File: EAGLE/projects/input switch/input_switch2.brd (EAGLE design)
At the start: 50 x 100 mm, 53 parts, among them U1 NE5532AD8G, U2 NE5532AD8G

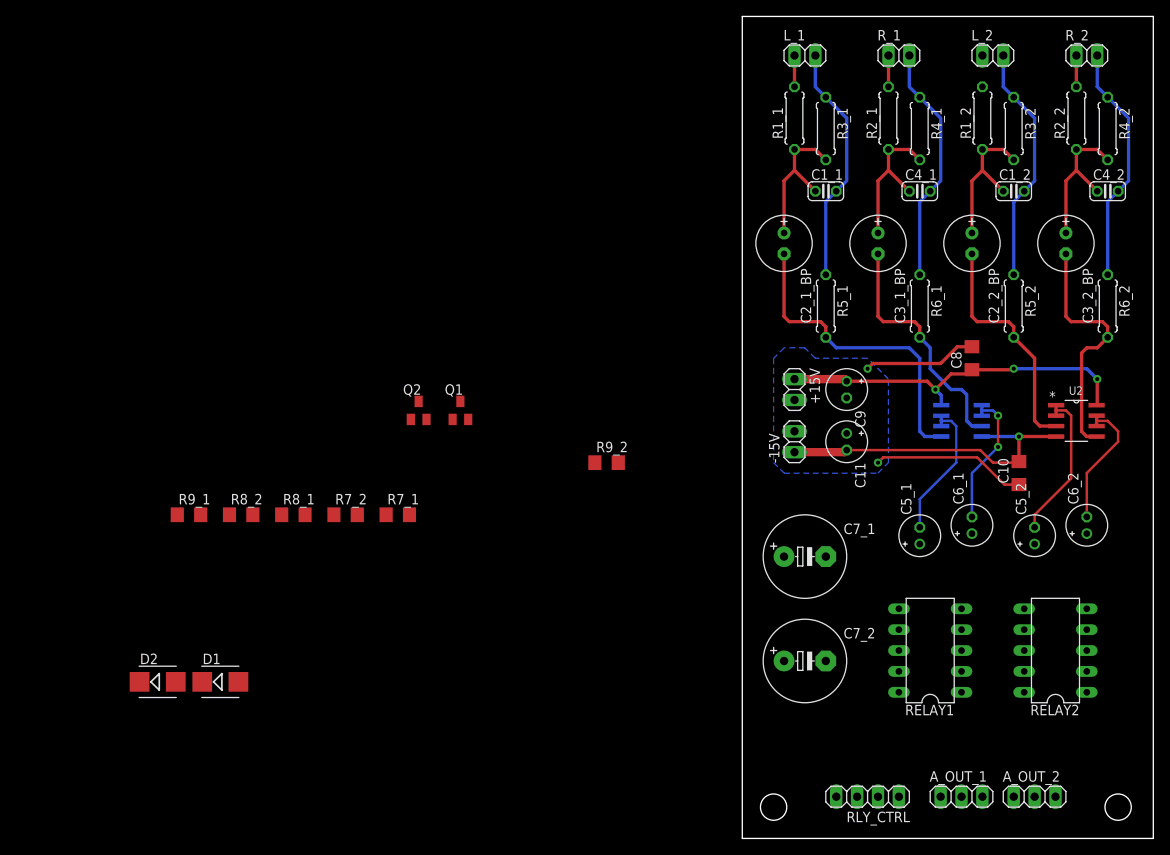
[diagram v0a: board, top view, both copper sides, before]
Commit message: DIP NE5532
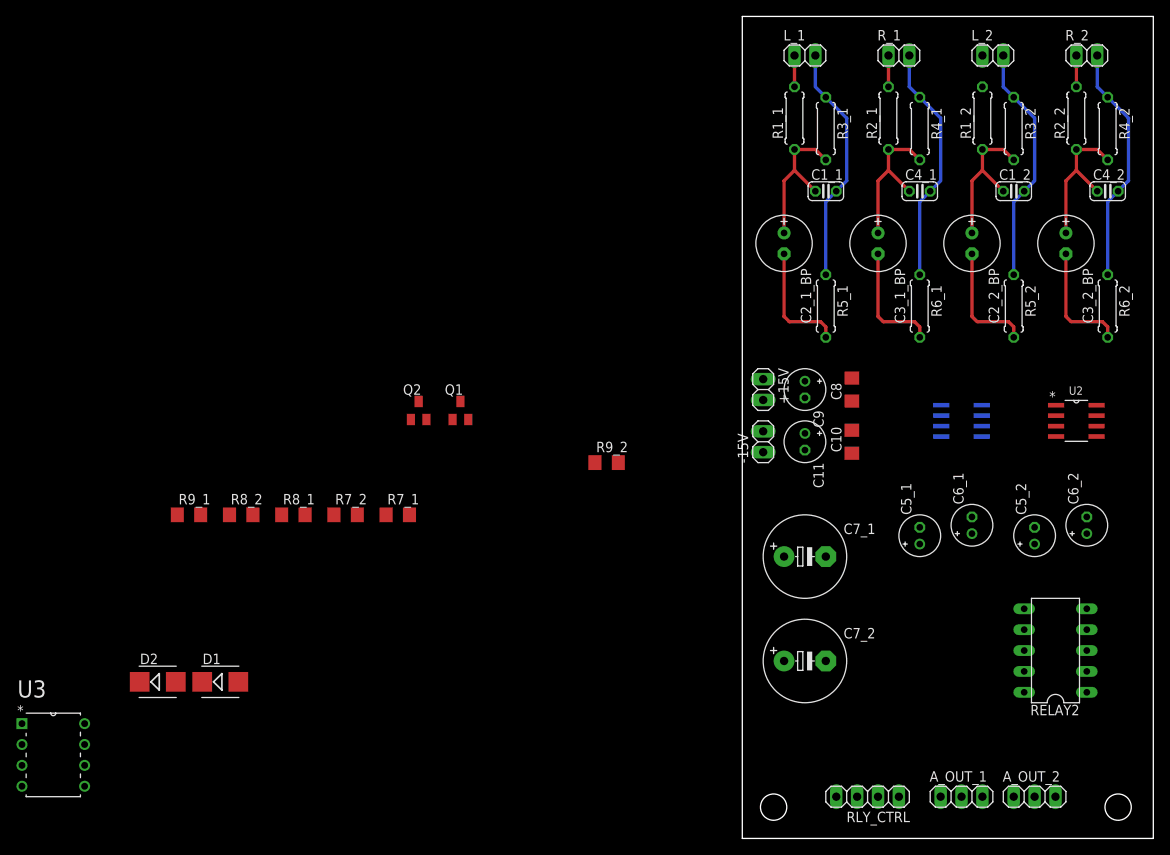
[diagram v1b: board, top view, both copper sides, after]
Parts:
- removed RELAY1: (no value), ic-package:DIL10
- added U3: NE5532P, ne5532:DIP254P762X508-8
- moved C10 20.7 mm to (13.3, 48.3)
- moved C8 15.1 mm to (13.3, 54.6)
- moved C11 5.08 mm to (7.62, 48.3)
- moved C9 5.08 mm to (7.62, 54.6)
- moved +15V 3.81 mm to (2.54, 54.6)
- moved -15V 3.81 mm to (2.54, 48.3)
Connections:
- removed net N$25: A_OUT_1.1, RELAY1.7
- removed net N$8: C6_1.+, RELAY1.3
- new net VCC+: U3.8
- new net VCC-: U3.4
- net N$11: no longer RELAY1.2
- net N$12: no longer RELAY1.9
- net N$18: no longer RELAY1.10
- net N$31: no longer RELAY1.8
- net N$37: no longer RELAY1.1
- net N$9: no longer RELAY1.4
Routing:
- net +15V: track 44.3 -> 0.00 mm, vias 3 -> 0
- net -15V: track 40.2 -> 0.00 mm, vias 1 -> 0
- net GND: track 149.8 -> 117.2 mm, vias 2 -> 0
- net N$4: track 38.7 -> 14.5 mm
- net N$13: track 18.8 -> 0.00 mm
- net N$5: track 17.5 -> 0.00 mm
- net N$7: track 17.1 -> 0.00 mm, vias 2 -> 0
- net N$10: track 16.4 -> 0.00 mm
- net N$26: track 30.1 -> 14.5 mm
- net N$20: track 29.9 -> 14.5 mm
- net N$27: track 28.6 -> 14.5 mm
- removed copper zone on layer 16, net GND

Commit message: input
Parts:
- removed C7_1, C7_2: 220u, rcl:E5-10,5
- removed U3: NE5532P, ne5532:DIP254P762X508-8
- added RELAY1: (no value), ic-package:DIL10
- added RGND1, RGND2, RGND3, RGND4: 10, rcl:R1206
- added R_PS1, R_PS2: 100, rcl:0207/7
- U1, U2: value NE5532AD8G -> NE5532P; device ne5532:SOIC127P600X175-8N -> ne5532:DIP254P762X508-8
- moved R8_2 112.9 mm to (47.0, 6.35), turned to 90 degrees
- moved D2 109.5 mm to (38.1, 26.7)
- moved R9_1 101.2 mm to (27.9, 5.08), turned to 90 degrees
- moved R8_1 90.1 mm to (29.2, 6.35), turned to 90 degrees
- moved R7_2 86.8 mm to (38.1, 30.5)
- moved D1 81.6 mm to (17.8, 26.7)
- moved R9_2 74.3 mm to (45.7, 5.08), turned to 90 degrees
- moved Q2 70.3 mm to (27.9, 31.8)
- moved Q1 67.7 mm to (27.9, 25.4)
- moved R7_1 60.3 mm to (17.8, 30.5)
- moved C5_1 22.2 mm to (43.2, 41.9)
- moved -15V 19.1 mm to (3.81, 29.2)
- moved C9 18.2 mm to (3.81, 36.8), turned to 0 degrees
- moved C6_2 18.2 mm to (24.1, 41.9)
- moved C10 12.3 mm to (8.89, 36.8), turned to 270 degrees
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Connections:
- removed net VCC+: U3.8
- removed net VCC-: U3.4
- new net AGND: A_OUT_1.2, A_OUT_2.2, C1_2.2, C4_1.2, C4_2.2, R3_2.1, R4_1.1, R4_2.1, R5_1.1, R5_2.1, R6_1.1, R6_2.1, RGND1.1, RGND2.1, RGND3.1, RGND4.1
- new net N$14: A_OUT_1.1, RELAY1.7
- new net N$17: -15V.1, R_PS2.2
- new net N$25: +15V.1, R_PS1.2
- new net N$33: L_1.2, RGND2.2
- new net N$36: RGND1.2, R_1.2
- new net N$41: C1_1.2, R3_1.1
- new net N$42: RGND3.2, R_2.2
- new net N$43: L_2.2, RGND4.2
- new net N$8: C6_1.+, RELAY1.3
- net +15V: now also R_PS1.1; no longer +15V.1
- net -15V: now also R_PS2.1; no longer -15V.1
- net GND: no longer A_OUT_1.2, A_OUT_2.2, C1_1.2, C1_2.2, C4_1.2, C4_2.2, L_1.2, L_2.2, R3_1.1, R3_2.1, R4_1.1, R4_2.1, R5_1.1, R5_2.1, R6_1.1, R6_2.1, R_1.2, R_2.2
- net N$11: now also RELAY1.2
- net N$12: now also RELAY1.9
- net N$18: now also RELAY1.10; no longer C7_1.-
- net N$31: now also RELAY1.8
- net N$37: now also RELAY1.1; no longer C7_1.+, C7_2.+
- net N$38: no longer C7_2.-
- net N$9: now also RELAY1.4
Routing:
- net GND: track 117.2 -> 0.00 mm
- net N$3: track 18.6 -> 0.00 mm
- net N$24: track 18.6 -> 0.00 mm
- net N$23: track 18.6 -> 0.00 mm
- net N$6: track 18.6 -> 0.00 mm
- net N$27: track 14.5 -> 0.00 mm
- net N$26: track 14.5 -> 0.00 mm
- net N$4: track 14.5 -> 0.00 mm
- net N$20: track 14.5 -> 0.00 mm
- net N$21: track 3.81 -> 0.00 mm
- net N$2: track 3.81 -> 0.00 mm
- net N$1: track 3.81 -> 0.00 mm
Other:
- board size 50 x 100 mm -> 49.5 x 99.7 mm

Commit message: Input Board done
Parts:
- added C1, C2: (no value), rcl:C1206
- added J1: J12MM, jumper:12
- added J2: J25MM, jumper:25
- added SJ1, SJ2, SJ3, SJ4: (no value), jumper:SJ
- moved R7_2 29.3 mm to (15.9, 11.4), turned to 270 degrees
- moved C10 24.3 mm to (11.4, 61.0), flipped to the bottom
- moved D2 24.2 mm to (14.0, 25.4), turned to 90 degrees
- moved R7_1 20.8 mm to (9.53, 11.4), turned to 270 degrees
- moved Q1 20.5 mm to (8.89, 17.8)
- moved Q2 18.9 mm to (15.2, 17.8)
- moved +15V 18.0 mm to (6.35, 33.0), turned to 180 degrees
- moved R_PS1 17.3 mm to (10.2, 44.5), turned to 270 degrees
- moved C9 16.7 mm to (6.35, 53.3), turned to 270 degrees
- moved C11 16.7 mm to (6.35, 59.7), turned to 270 degrees
- moved R_PS2 14.5 mm to (5.08, 44.5), turned to 270 degrees
- moved R9_2 13.5 mm to (36.8, 15.2), flipped to the bottom
- moved C5_1 13.0 mm to (30.5, 44.5)
- moved C5_2 13.0 mm to (43.2, 44.5)
- moved C6_1 13.0 mm to (24.1, 44.5)
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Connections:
- new net N$44: J2.2, RELAY2.10
- net +15V: now also C1.1
- net -15V: now also C2.2
- net AGND: now also C1_1.2, R3_1.1, R8_1.1, R8_2.1, R9_1.1, R9_2.1, SJ1.1, SJ1.2, SJ2.1, SJ2.2, SJ3.1, SJ3.2, SJ4.1, SJ4.2
- net GND: now also C1.2, C2.1; no longer R8_1.1, R8_2.1, R9_1.1, R9_2.1
- net N$37: now also J1.2; no longer RELAY2.1
- net N$38: now also J2.1; no longer RELAY2.10
- net N$41: now also J1.1, RELAY2.1; no longer C1_1.2, R3_1.1
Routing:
- net AGND: track 0.00 -> 240.5 mm
- net GND: track 0.00 -> 67.9 mm, vias 0 -> 1
- net N$37: track 0.00 -> 67.2 mm, vias 0 -> 1
- net -15V: track 0.00 -> 62.5 mm
- net +15V: track 0.00 -> 51.6 mm, vias 0 -> 2
- net N$18: track 0.00 -> 36.6 mm, vias 0 -> 1
- net N$27: track 0.00 -> 29.1 mm
- net N$4: track 0.00 -> 28.8 mm
- net N$10: track 0.00 -> 24.3 mm
- net N$40: track 0.00 -> 22.5 mm, vias 0 -> 2
- net N$31: track 0.00 -> 21.2 mm
- net N$38: track 0.00 -> 20.5 mm
- net N$7: track 0.00 -> 20.2 mm
- net N$30: track 0.00 -> 20.2 mm
- net N$29: track 0.00 -> 20.1 mm
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
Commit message: a lot
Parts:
- removed SJ1, SJ2, SJ3, SJ4: (no value), jumper:SJ
- added R1: 100, rcl:R1206
- moved R4_1 2.01 mm to (18.4, 85.7)
- moved C4_1 1.91 mm to (17.1, 77.5)
- moved R2_1 1.91 mm to (14.6, 85.1)
- moved R3_2 1.91 mm to (33.7, 85.1)
- moved C1_2 1.90 mm to (32.4, 77.5)
- moved R1_2 1.90 mm to (29.8, 85.1)
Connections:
- net AGND: now also R1.1; no longer SJ1.1, SJ1.2, SJ2.1, SJ2.2, SJ3.1, SJ3.2, SJ4.1, SJ4.2
- net GND: now also R1.2
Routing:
- net AGND: track 240.5 -> 252.5 mm
- net GND: track 67.9 -> 79.4 mm
- net +15V: track 51.6 -> 57.6 mm
- net N$1: track 4.44 -> 5.61 mm
- net N$23: track 13.5 -> 14.5 mm
- net N$22: track 4.44 -> 5.23 mm
- net N$10: track 24.3 -> 25.1 mm
- net -15V: track 62.5 -> 63.2 mm
- net N$6: track 13.5 -> 13.0 mm

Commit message: stuff
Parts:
- R8_1, R8_2, R9_1, R9_2: value 220k -> 330k
- renumbered A_OUT_1 to OUT1, A_OUT_2 to OUT2, L_1 to LEFT1, L_2 to LEFT2, R_1 to RIGHT1, R_2 to RIGHT2
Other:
- board text added: "5V"
- board text added: "GND"
- board text added: "IN"
- board text added: "L"
- board text added: "R"
- board text added: "R1"
- board text added: "R2"
